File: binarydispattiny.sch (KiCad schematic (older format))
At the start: 32 parts, among them J1 Conn_01x02_Male, J2 Conn_01x08, J3 AVR-TPI-6, Q1 DMMT5401, U1 4021, U2 ATtiny102-SS, U3 19x12mm 7segment, U4 MAX7219, U5 19x12mm 7segment

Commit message: Fixed MAX7912 sizing
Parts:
- C1: footprint Capacitor_SMD:C_1206_3216Metric_Pad1.42x1.75mm_HandSolder -> Capacitor_SMD:CP_Elec_5x5.4; symbol Device:C -> Device:CP
- RN1, RN2: footprint Resistor_SMD:R_Array_Convex_4x1206 -> Resistor_SMD:R_Array_Convex_4x0603
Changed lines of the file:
@@
 F 0 "RN2" H 2688 6896 50  0000 L CNN
 F 1 "330" H 2688 6805 50  0000 L CNN
-F 2 "Resistor_SMD:R_Array_Convex_4x1206" V 2775 6850 50  0001 C CNN
+F 2 "Resistor_SMD:R_Array_Convex_4x0603" V 2775 6850 50  0001 C CNN
 F 3 "~" H 2500 6850 50  0001 C CNN
 	1    2500 6850
@@
 F 0 "RN1" H 2050 6150 50  0000 L CNN
 F 1 "330" H 2050 6050 50  0000 L CNN
-F 2 "Resistor_SMD:R_Array_Convex_4x1206" V 2775 6100 50  0001 C CNN
+F 2 "Resistor_SMD:R_Array_Convex_4x0603" V 2775 6100 50  0001 C CNN
 F 3 "~" H 2500 6100 50  0001 C CNN
 	1    2500 6100
@@
 	7000 4700 7350 4700
 $Comp
-L Device:C C1
+L Device:CP C1
 U 1 1 5EB4D9D4
 P 1950 1450
 F 0 "C1" H 2065 1496 50  0000 L CNN
 F 1 "10uF" H 2065 1405 50  0000 L CNN
-F 2 "Capacitor_SMD:C_1206_3216Metric_Pad1.42x1.75mm_HandSolder" H 1988 1300 50  0001 C CNN
+F 2 "Capacitor_SMD:CP_Elec_5x5.4" H 1988 1300 50  0001 C CNN
 F 3 "~" H 1950 1450 50  0001 C CNN
 	1    1950 1450

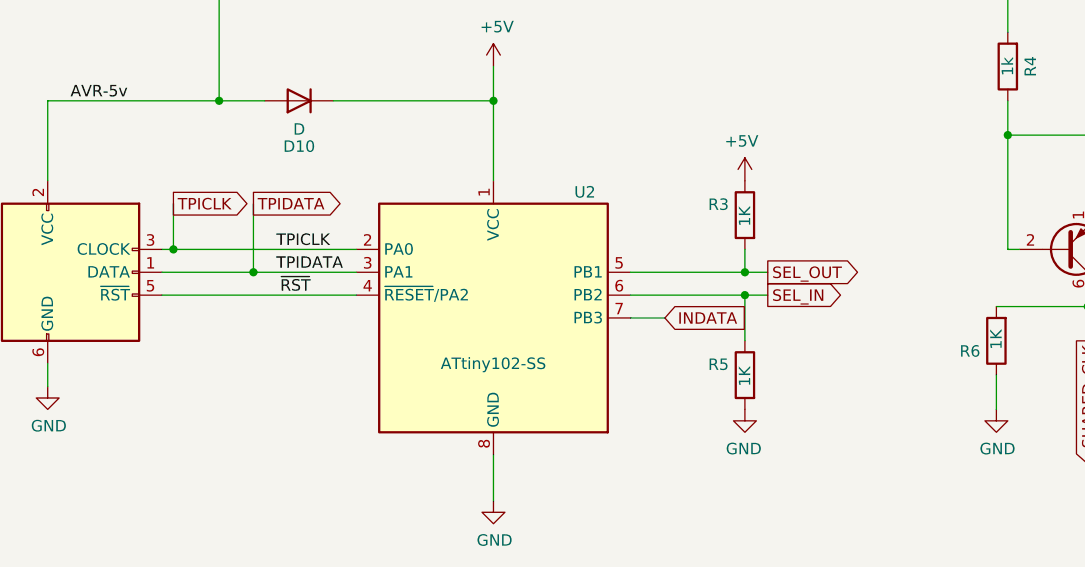
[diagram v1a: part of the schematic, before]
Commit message: Added test points
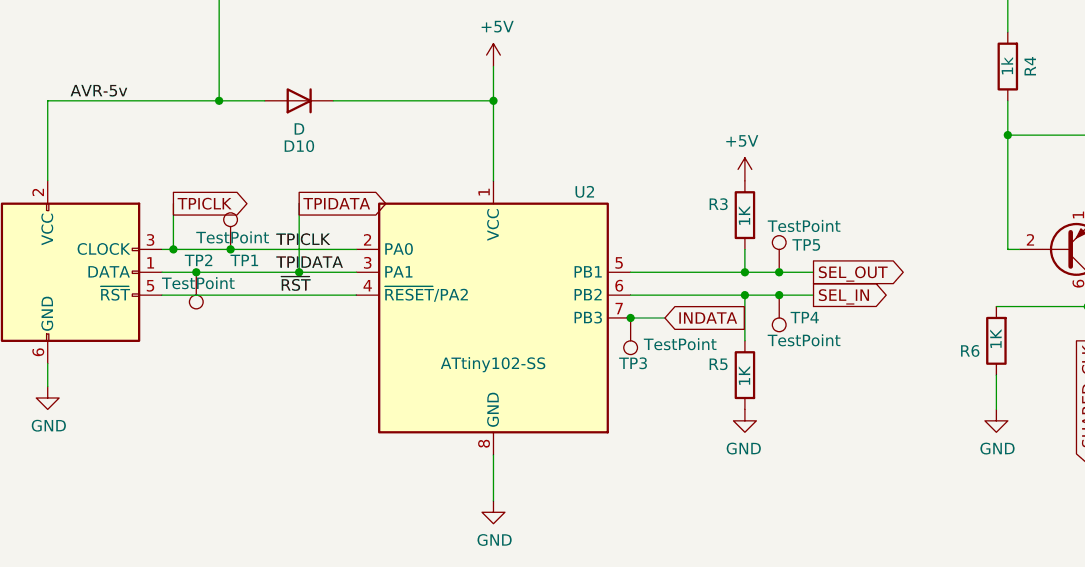
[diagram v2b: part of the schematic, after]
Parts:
- added TP1, TP2, TP3, TP4, TP5: TestPoint, TestPoint:TestPoint_Pad_1.0x1.0mm, symbol Connector:TestPoint
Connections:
- net INDATA: now also TP3.1
- net SEL_IN: now also TP4.1
- net SEL_OUT: now also TP5.1
- net TPICLK: now also TP1.1
- net TPIDATA: now also TP2.1
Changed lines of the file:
@@
 Text Label 5200 2050 2    50   ~ 0
 ~RST
-Text GLabel 7200 1950 2    50   Output ~ 0
+Text GLabel 7400 1950 2    50   Output ~ 0
 SEL_OUT
 Text GLabel 6000 5500 0    50   Input ~ 0
@@
 INDATA
 Wire Wire Line
-	7200 1950 7100 1950
+	7400 1950 7250 1950
 Text GLabel 1900 3800 0    50   Input ~ 0
 SHARED_CLK
@@
 Wire Wire Line
 	1900 4100 2150 4100
-Text GLabel 7200 2050 2    50   Output ~ 0
+Text GLabel 7400 2050 2    50   Output ~ 0
 SEL_IN
 Wire Wire Line
-	7200 2050 7100 2050
+	7400 2050 7250 2050
 $Comp
 L power:PWR_FLAG #FLG0101
@@
 	7100 1850 7100 1950
 Connection ~ 7100 1950
-Wire Wire Line
-	7100 1950 6600 1950
 $Comp
 L Device:R R5
@@
 Connection ~ 4600 1850
 Wire Wire Line
-	4600 1850 5400 1850
-Text GLabel 4950 1650 2    50   Output ~ 0
+	4600 1850 4850 1850
+Text GLabel 5150 1650 2    50   Output ~ 0
 TPIDATA
 Wire Wire Line
-	4950 1650 4950 1950
-Connection ~ 4950 1950
-Wire Wire Line
-	4950 1950 5400 1950
+	5150 1650 5150 1950
 Text GLabel 9550 1500 2    50   Input ~ 0
 TPIDATA
@@
 	4550 2050 5400 2050
 Wire Wire Line
-	4550 1950 4950 1950
+	4550 1950 4700 1950
 Wire Wire Line
 	4550 1850 4600 1850
@@
 	7100 2250 7100 2050
 Connection ~ 7100 2050
-Wire Wire Line
-	7100 2050 6600 2050
 Wire Wire Line
 	7000 4100 7350 4100
@@
 	10150 1350 10150 1450
 Connection ~ 9250 1350
+$Comp
+L Connector:TestPoint TP1
+U 1 1 5EDCDBBA
+P 4850 1850
+F 0 "TP1" H 4850 1800 50  0000 L CNN
+F 1 "TestPoint" H 4700 1900 50  0000 L CNN
+F 2 "TestPoint:TestPoint_Pad_1.0x1.0mm" H 5050 1850 50  0001 C CNN
+F 3 "~" H 5050 1850 50  0001 C CNN
+	1    4850 1850
+	1    0    0    -1
+$EndComp
+Connection ~ 4850 1850
+Wire Wire Line
+	4850 1850 5400 1850
+$Comp
+L Connector:TestPoint TP2
+U 1 1 5EDCF7C4
+P 4700 1950
+F 0 "TP2" H 4750 1900 50  0000 R CNN
+F 1 "TestPoint" H 4850 2000 50  0000 R CNN
+F 2 "TestPoint:TestPoint_Pad_1.0x1.0mm" H 4900 1950 50  0001 C CNN
+F 3 "~" H 4900 1950 50  0001 C CNN
+	1    4700 1950
+	-1   0    0    1
+$EndComp
+Connection ~ 4700 1950
+Wire Wire Line
+	4700 1950 5150 1950
+$Comp
+L Connector:TestPoint TP5
+U 1 1 5EDCFFAA
+P 7250 1950
+F 0 "TP5" H 7308 2068 50  0000 L CNN
+F 1 "TestPoint" H 7200 2150 50  0000 L CNN
+F 2 "TestPoint:TestPoint_Pad_1.0x1.0mm" H 7450 1950 50  0001 C CNN
+F 3 "~" H 7450 1950 50  0001 C CNN
+	1    7250 1950
+	1    0    0    -1
+$EndComp
+$Comp
+L Connector:TestPoint TP4
+U 1 1 5EDD0674
+P 7250 2050
+F 0 "TP4" H 7200 2150 50  0000 R CNN
+F 1 "TestPoint" H 7300 2250 50  0000 R CNN
+F 2 "TestPoint:TestPoint_Pad_1.0x1.0mm" H 7450 2050 50  0001 C CNN
+F 3 "~" H 7450 2050 50  0001 C CNN
+	1    7250 2050
+	-1   0    0    1
+$EndComp
+$Comp
+L Connector:TestPoint TP3
+U 1 1 5EDD0C6B
+P 6600 2150
+F 0 "TP3" H 6650 2350 50  0000 R CNN
+F 1 "TestPoint" H 6542 2267 50  0000 R CNN
+F 2 "TestPoint:TestPoint_Pad_1.0x1.0mm" H 6800 2150 50  0001 C CNN
+F 3 "~" H 6800 2150 50  0001 C CNN
+	1    6600 2150
+	-1   0    0    1
+$EndComp
+Connection ~ 6600 2150
+Connection ~ 7250 1950
+Wire Wire Line
+	7250 1950 7100 1950
+Wire Wire Line
+	6600 1950 7100 1950
+Connection ~ 7250 2050
+Wire Wire Line
+	7250 2050 7100 2050
+Wire Wire Line
+	6600 2050 7100 2050
+Connection ~ 5150 1950
+Wire Wire Line
+	5150 1950 5400 1950
 $EndSCHEMATC
